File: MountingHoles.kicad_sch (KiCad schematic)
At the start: 12 parts

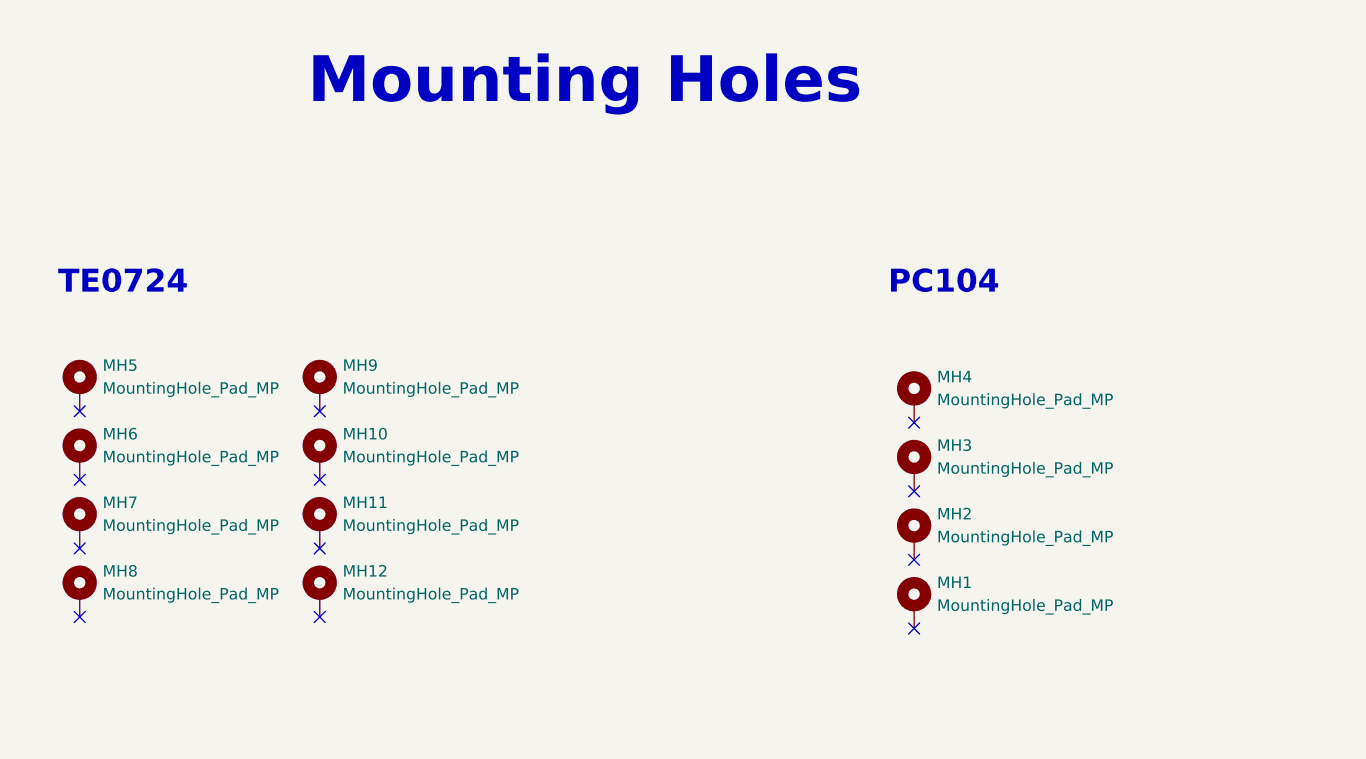
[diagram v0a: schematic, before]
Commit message: Fixed GND issues with connector and mounting holes
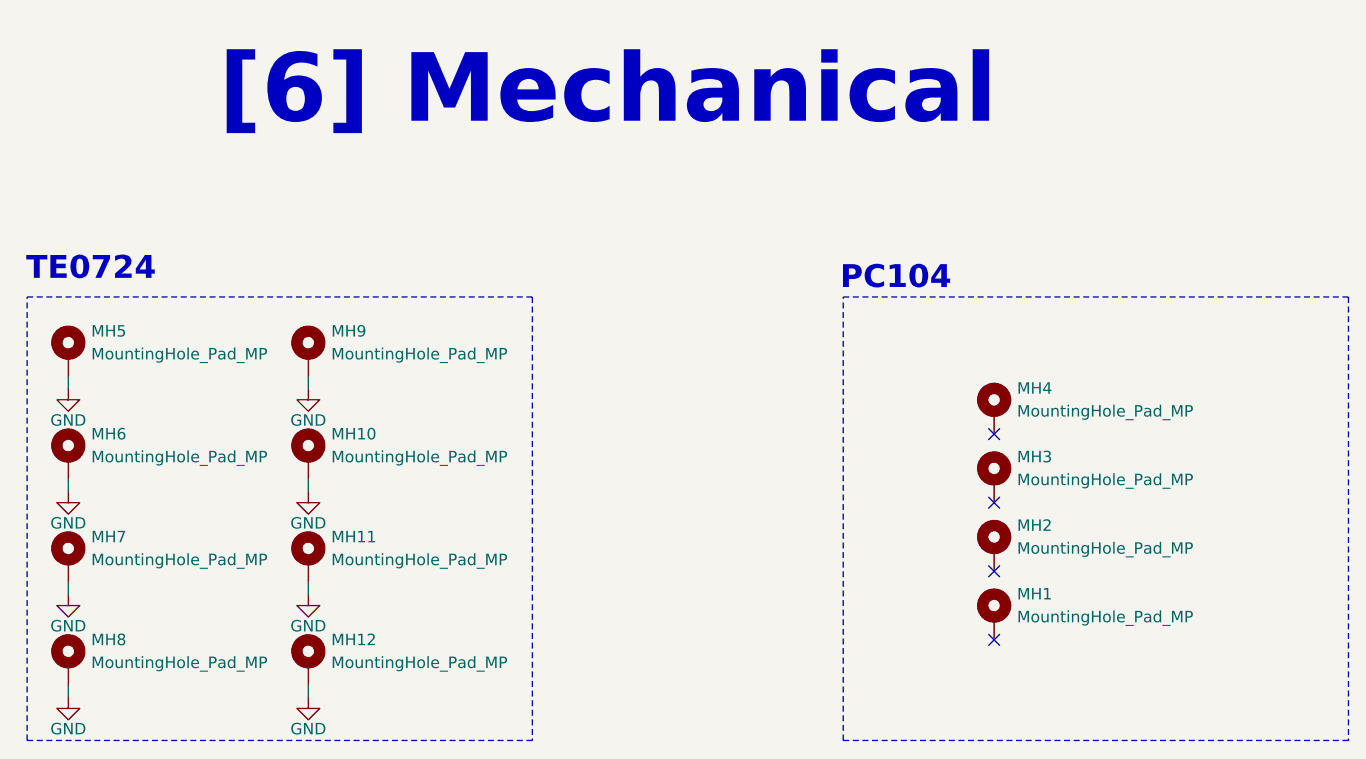
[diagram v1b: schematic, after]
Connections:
- net GND: now reaches MH7.MP
- net GND: now also MH10.MP, MH11.MP, MH12.MP, MH5.MP, MH6.MP, MH8.MP, MH9.MP
- no-connect marks 12 -> 4
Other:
- note added: "[6] Mechanical"
- note removed: "Mounting Holes"
- moved on the sheet: MH1, MH10, MH11, MH12, MH2, MH3, MH4, MH5, MH6, MH7, MH8, MH9
